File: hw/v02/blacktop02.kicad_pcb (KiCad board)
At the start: 2 copper layers, 50.8 x 33 mm, 13 parts, among them J1 Conn_01x10_Female_Left, J2 Conn_01x10_Female_Right, SW1 EVQ-Q2Y03W, U1 MSP430G2553IPW28, U2 AT25640B-SSHL-T, U3 HDSM-283L, U4 HDSM-283L, U5 HDSM-283L, U6 HDSM-283L

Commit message: v03 RC1 (rename is nontrivial so use v02 dir)
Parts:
- added FID1: Fiducial, Fiducial:Fiducial_0.75mm_Mask1.5mm, F.Cu at (129.9, 100.0)
- added FID2: Fiducial, Fiducial:Fiducial_0.75mm_Mask1.5mm, F.Cu at (166.4, 100.0)
- added FID3: Fiducial, Fiducial:Fiducial_0.75mm_Mask1.5mm, F.Cu at (166.4, 70.2)
- moved REF** 2.01 mm to (169.2, 95.2)
- moved SW1 0.90 mm to (166.5, 76.4)
- moved C2 0.64 mm to (158.4, 71.1)
- moved U2 0.25 mm to (159.4, 75.9)
- moved C1 0.15 mm to (141.6, 71.1)
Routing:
- net VCC: track 4.65 -> 42.2 mm
- net /P1.6: track 62.6 -> 56.0 mm
- net (no net): track 0.00 -> 4.01 mm
- net /RGB_B: track 60.4 -> 57.8 mm
- net /~CS: track 41.2 -> 43.6 mm
- net GND: track 15.1 -> 13.1 mm
- net /BTN: track 35.2 -> 34.4 mm
- net /SOMI: track 25.7 -> 25.1 mm
- net /RGB_G: track 68.0 -> 68.4 mm, vias 0 -> 1
- removed copper zone on F.Cu, net VCC
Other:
- outline, holes or cut-outs redrawn
- board text added: "v03"
- board text removed: "v02"

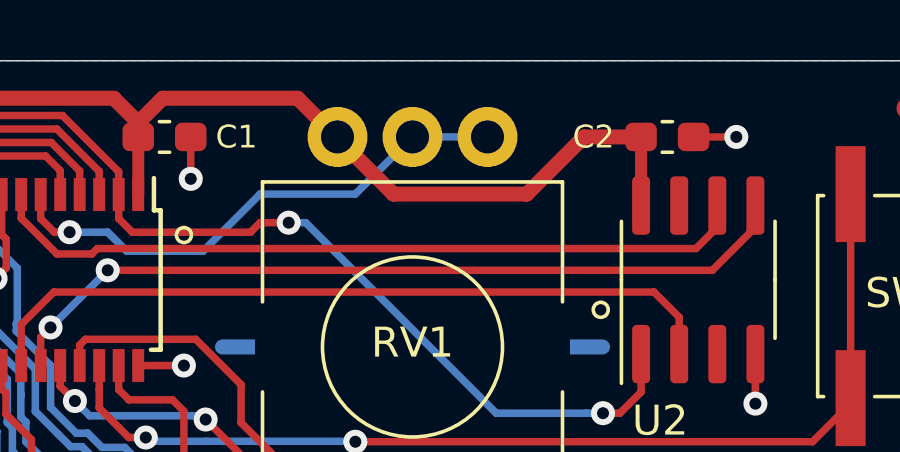
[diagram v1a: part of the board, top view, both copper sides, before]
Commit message: moved RV1 pin3 from pin2 to GND
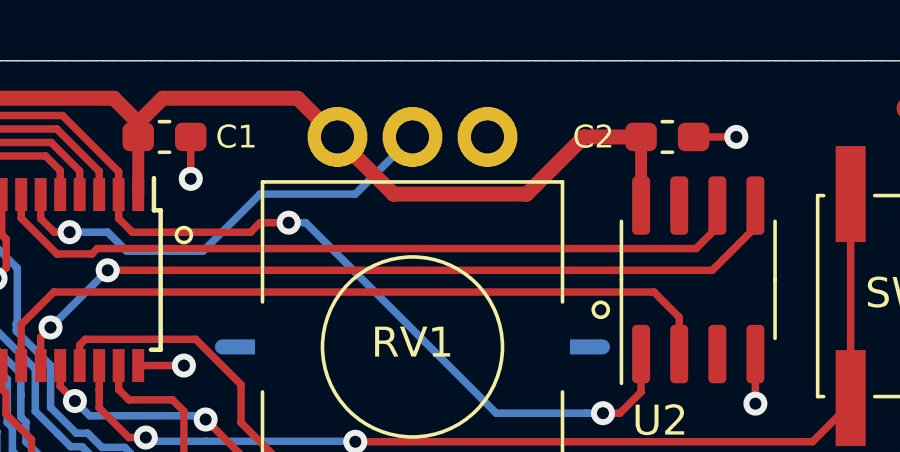
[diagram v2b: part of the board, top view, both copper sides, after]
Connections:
- RV1 pad 1: /POT -> GND
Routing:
- net GND: track 13.1 -> 17.1 mm
- net (no net): track 4.01 -> 0.00 mm
- net /POT: track 17.7 -> 15.2 mm
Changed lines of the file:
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@@
     (thickness 1.6)
     (drawings 11)
-    (tracks 406)
+    (tracks 405)
     (zones 0)
     (modules 16)
@@
       (net 21 /POT))
     (pad 1 thru_hole circle (at -2.5 7 180) (size 2 2) (drill 1.1) (layers *.Cu *.Mask)
-      (net 21 /POT))
+      (net 2 GND))
     (pad "" np_thru_hole roundrect (at 4.35 0 180) (size 1.9 2.3) (drill oval 1.8 2.2) (layers *.Cu *.Mask) (roundrect_rratio 0.289))
     (pad "" np_thru_hole roundrect (at -4.35 0 180) (size 1.9 2.3) (drill oval 1.8 2.2) (layers *.Cu *.Mask) (roundrect_rratio 0.289))
@@
     (effects (font (size 1 1) (thickness 0.15)) (justify left))
   )
-  (segment (start 143.525 78.12) (end 145.51 78.12) (width 0.5) (layer B.Cu) (net 0))
-  (segment (start 143.51 78.105) (end 143.525 78.12) (width 0.25) (layer B.Cu) (net 0))
-  (segment (start 156.195 78.12) (end 154.21 78.12) (width 0.5) (layer B.Cu) (net 0))
-  (segment (start 156.21 78.105) (end 156.195 78.12) (width 0.25) (layer B.Cu) (net 0))
+  (segment (start 143.525 78.12) (end 145.51 78.12) (width 0.5) (layer B.Cu) (net 2))
+  (segment (start 143.51 78.105) (end 143.525 78.12) (width 0.25) (layer B.Cu) (net 2))
+  (segment (start 156.195 78.12) (end 154.21 78.12) (width 0.5) (layer B.Cu) (net 2))
+  (segment (start 156.21 78.105) (end 156.195 78.12) (width 0.25) (layer B.Cu) (net 2))
   (segment (start 146.029963 69.829963) (end 149.225 73.025) (width 0.5) (layer F.Cu) (net 1))
   (segment (start 155.575 71.12) (end 157.48 71.12) (width 0.5) (layer F.Cu) (net 1))
@@
   (segment (start 137.921 74.295) (end 138.43 74.295) (width 0.25) (layer F.Cu) (net 21))
   (segment (start 138.43 74.295) (end 139.7 74.295) (width 0.25) (layer B.Cu) (net 21))
-  (segment (start 149.86 71.12) (end 152.36 71.12) (width 0.25) (layer B.Cu) (net 21))
   (via (at 140.97 81.139119) (size 0.8) (drill 0.4) (layers F.Cu B.Cu) (net 22))
   (segment (start 142.976161 81.26349) (end 141.094371 81.26349) (width 0.25) (layer B.Cu) (net 22))

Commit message: v03 final, prototypes ordered 2020-02-17
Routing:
- net GND: track 17.1 -> 13.1 mm
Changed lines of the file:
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@@
     (thickness 1.6)
     (drawings 11)
-    (tracks 405)
+    (tracks 403)
     (zones 0)
     (modules 16)
@@
     (effects (font (size 1 1) (thickness 0.15)) (justify left))
   )
-  (segment (start 143.525 78.12) (end 145.51 78.12) (width 0.5) (layer B.Cu) (net 2))
   (segment (start 143.51 78.105) (end 143.525 78.12) (width 0.25) (layer B.Cu) (net 2))
-  (segment (start 156.195 78.12) (end 154.21 78.12) (width 0.5) (layer B.Cu) (net 2))
   (segment (start 156.21 78.105) (end 156.195 78.12) (width 0.25) (layer B.Cu) (net 2))
   (segment (start 146.029963 69.829963) (end 149.225 73.025) (width 0.5) (layer F.Cu) (net 1))
